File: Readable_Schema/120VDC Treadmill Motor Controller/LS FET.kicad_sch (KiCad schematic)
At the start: 5 parts, among them Q2 IRFB4227PBF, U2 FOD3182

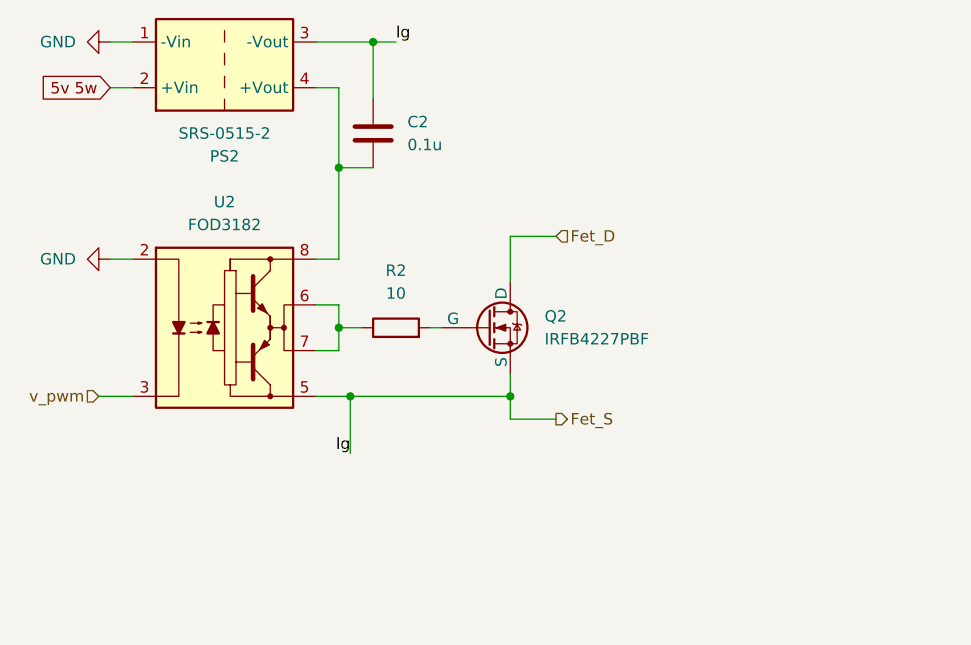
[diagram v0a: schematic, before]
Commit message: Updated some more footprints and started learning about base resistor sizing and the importance of Pavg rather than Ppeak. changed low side fets in kicad to use a shared power supply
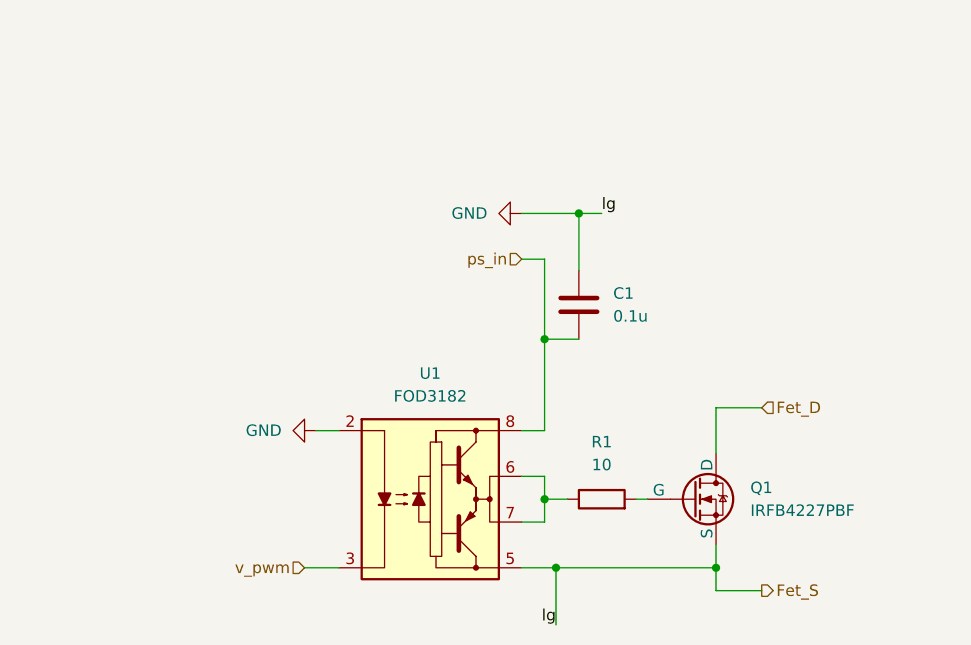
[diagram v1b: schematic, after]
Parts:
- removed C2: 0.1u, Capacitor_SMD:C_0402_1005Metric_Pad0.74x0.62mm_HandSolder, symbol Device:C
- removed PS2: SRS-0515-2, Footprints_TMC:SRS-0515 DIP-16_W7.62mm, symbol Converter_DCDC:MEE1S0303SC
- removed Q2: IRFB4227PBF, Package_TO_SOT_THT:TO-220-3_Vertical, symbol Simulation_SPICE:NMOS
- removed R2: 10, symbol Device:R
- removed U2: FOD3182, Package_DIP:DIP-8_W7.62mm, symbol Driver_FET:TLP250
- added C1: 0.1u, Capacitor_SMD:C_0402_1005Metric_Pad0.74x0.62mm_HandSolder, symbol Device:C
- added Q1: IRFB4227PBF, Package_TO_SOT_THT:TO-220-3_Vertical, symbol Simulation_SPICE:NMOS
- added R1: 10, symbol Device:R
- added U1: FOD3182, Package_DIP:DIP-8_W7.62mm, symbol Driver_FET:TLP250
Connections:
- net Fet_D: now also Q1.1 (D)
- net GND: now also C1.1, Q1.3 (S), U1.2 (A), U1.5 (VEE)
- net v_pwm: now also U1.3 (C)
- new net: R1.1, U1.6 (VO), U1.7 (VO)
- new net: Q1.2 (G), R1.2
- new net ps_in: C1.2, U1.8 (VCC)

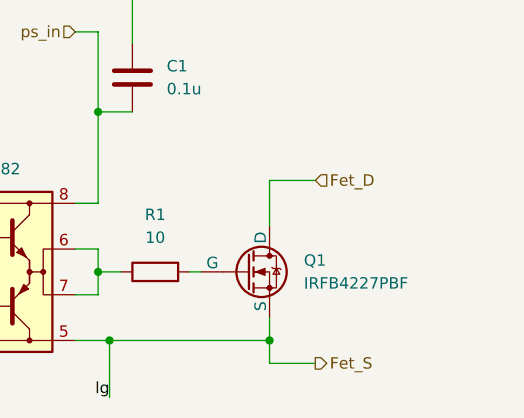
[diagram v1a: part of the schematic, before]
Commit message: Continuing to update footprints, did some follow up math on low pass filter for adc voltage coming out of current sense system
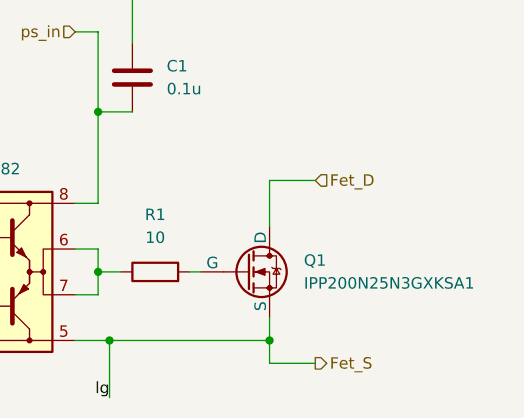
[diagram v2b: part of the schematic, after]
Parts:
- Q1: value IRFB4227PBF -> IPP200N25N3GXKSA1
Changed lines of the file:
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@@
 			(project ""
 				(path "/319bc5c0-2dd5-4df3-a34b-9170833ebccd/49a5a11b-8174-445d-b343-1fe5ec8c60de/c56e55f9-2f01-4a9a-a881-dd8c5892be8d"
-					(reference "#PWR07")
+					(reference "#PWR0103")
 					(unit 1)
 				)
@@
 			)
 		)
-		(property "Value" "IRFB4227PBF"
+		(property "Value" "IPP200N25N3GXKSA1"
 			(at 168.91 113.0299 0)
 			(effects
@@
 			)
 		)
-		(property "Datasheet" "https://www.infineon.com/assets/row/public/documents/24/49/infineon-irfb4227-datasheet-en.pdf"
+		(property "Datasheet" "https://www.infineon.com/assets/row/public/documents/24/49/infineon-ipp-b-i-200n25n3-g-datasheet-en.pdf?folderId=db3a3043163797a6011637d4bae7003b&fileId=db3a3043243b5f17012496b87e9f1971"
 			(at 162.56 124.46 0)
 			(effects

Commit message: continued to add footprints, we still need to add hall effect circuit and possible brake resistor subcircuit. We may also want to consider switching the large 15v isolated power supplies to be smd as well as the FOD3182. Otherwise this will become a lot to hand solder.
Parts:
- R1: footprint (none) -> Resistor_SMD:R_0201_0603Metric_Pad0.64x0.40mm_HandSolder
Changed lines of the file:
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@@
+	)
+	(symbol
+		(lib_id "Device:R")
+		(at 152.4 111.76 90)
+		(unit 1)
+		(exclude_from_sim no)
+		(in_bom yes)
+		(on_board yes)
+		(dnp no)
+		(fields_autoplaced yes)
+		(property "Reference" "R1"
+			(at 152.4 105.41 90)
+			(effects
+				(font
+					(size 1.27 1.27)
+				)
+			)
+		)
+		(property "Value" "10"
+			(at 152.4 107.95 90)
+			(effects
+				(font
+					(size 1.27 1.27)
+				)
+			)
+		)
+		(property "Footprint" "Resistor_SMD:R_0201_0603Metric_Pad0.64x0.40mm_HandSolder"
+			(at 152.4 113.538 90)
+			(effects
+				(font
+					(size 1.27 1.27)
+				)
+				(hide yes)
+			)
+		)
+		(property "Datasheet" "https://industrial.panasonic.com/cdbs/www-data/pdf/RDP0000/AOA0000C337.pdf"
+			(at 152.4 111.76 0)
+			(effects
+				(font
+					(size 1.27 1.27)
+				)
+				(hide yes)
+			)
+		)
+		(property "Description" "ERJ-UP3J100V"
+			(at 152.4 111.76 0)
+			(effects
+				(font
+					(size 1.27 1.27)
+				)
+				(hide yes)
+			)
+		)
+		(pin "1"
+		)
+		(pin "2"
+		)
+		(instances
+			(project "120VDC Treadmill Motor Controller"
+				(path "/319bc5c0-2dd5-4df3-a34b-9170833ebccd/49a5a11b-8174-445d-b343-1fe5ec8c60de/c56e55f9-2f01-4a9a-a881-dd8c5892be8d"
+					(reference "R6")
+					(unit 1)
+				)
+				(path "/319bc5c0-2dd5-4df3-a34b-9170833ebccd/49a5a11b-8174-445d-b343-1fe5ec8c60de/c8d3f65d-c1e4-4ff7-87e3-3541d9f7f8fc"
+					(reference "R1")
+					(unit 1)
+				)
+			)
+		)
 	)
 	(symbol
@@
 					(unit 1)
 				)
-			)
-		)
-	)
-	(symbol
-		(lib_id "Device:R")
-		(at 152.4 111.76 90)
-		(unit 1)
-		(exclude_from_sim no)
-		(in_bom yes)
-		(on_board yes)
-		(dnp no)
-		(fields_autoplaced yes)
-		(property "Reference" "R1"
-			(at 152.4 105.41 90)
-			(effects
-				(font
-					(size 1.27 1.27)
-				)
-			)
-		)
-		(property "Value" "10"
-			(at 152.4 107.95 90)
-			(effects
-				(font
-					(size 1.27 1.27)
-				)
-			)
-		)
-		(property "Footprint" ""
-			(at 152.4 113.538 90)
-			(effects
-				(font
-					(size 1.27 1.27)
-				)
-				(hide yes)
-			)
-		)
-		(property "Datasheet" "~"
-			(at 152.4 111.76 0)
-			(effects
-				(font
-					(size 1.27 1.27)
-				)
-				(hide yes)
-			)
-		)
-		(property "Description" "Resistor"
-			(at 152.4 111.76 0)
-			(effects
-				(font
-					(size 1.27 1.27)
-				)
-				(hide yes)
-			)
-		)
-		(pin "1"
-		)
-		(pin "2"
-		)
-		(instances
-			(project "120VDC Treadmill Motor Controller"
-				(path "/319bc5c0-2dd5-4df3-a34b-9170833ebccd/49a5a11b-8174-445d-b343-1fe5ec8c60de/c56e55f9-2f01-4a9a-a881-dd8c5892be8d"
-					(reference "R6")
-					(unit 1)
-				)
-				(path "/319bc5c0-2dd5-4df3-a34b-9170833ebccd/49a5a11b-8174-445d-b343-1fe5ec8c60de/c8d3f65d-c1e4-4ff7-87e3-3541d9f7f8fc"
-					(reference "R1")
-					(unit 1)
-				)
